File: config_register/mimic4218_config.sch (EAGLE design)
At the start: 19 parts, among them P5 44PINEDGE, U1 CD74HCT123, U2 CD74HCT123, U3 CD74HC573E, U4 CD74HC573E

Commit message: update netlist
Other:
- note added: "X_INTEN, U_INTEN, J_INTEN and ITENSIFY the cathode voltage. Low Levels bring the cathode negative. When Intensity is brought high the lectron gun will pulse"
- note added: "input"
- note added: "output"
- note added: "scale"
- note removed: "When high INTENSIFY will pulse the electron gun."
- note removed: "X_INTEN, U_INTEN, J_INTEN set the cathode voltage when the electron gun is on. Logic lows bring the cathode most negative."
- moved on the sheet: P5
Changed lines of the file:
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@@
 <text x="403.86" y="302.26" size="1.9304" layer="91" ratio="10">The J_JUMP, K_JUMP, L_JUMP bits bus to the Contra_1579 cards.
 Low levels on these lines enable current.</text>
-<text x="403.86" y="312.42" size="1.9304" layer="91" ratio="10">The DELAY_SELECT bit selects the 35 uS delay when high
+<text x="403.86" y="320.04" size="1.9304" layer="91" ratio="10">The DELAY_SELECT bit selects the 35 uS delay when high
 and the 1 uS delay when low.</text>
-<text x="403.86" y="322.58" size="1.9304" layer="91" ratio="10">When high INTENSIFY will pulse the electron gun.</text>
-<text x="403.86" y="330.2" size="1.9304" layer="91" ratio="10">X_INTEN, U_INTEN, J_INTEN set the cathode voltage
-when the electron gun is on.  Logic lows bring the
-cathode most negative.</text>
+<text x="403.86" y="330.2" size="1.9304" layer="91" ratio="10">X_INTEN, U_INTEN, J_INTEN and ITENSIFY the cathode voltage.
+Low Levels bring the cathode negative.
+When Intensity is brought high the lectron gun will pulse</text>
+<text x="134.62" y="337.82" size="1.778" layer="91">output</text>
+<text x="78.74" y="337.82" size="1.778" layer="91">input</text>
+<text x="134.62" y="337.82" size="1.778" layer="91">output</text>
+<text x="149.86" y="297.18" size="1.778" layer="91">scale</text>
+<text x="149.86" y="274.32" size="1.778" layer="91">scale</text>
 </plain>
 <instances>
@@
 <instance part="FRAME1" gate="G$1" x="0" y="0"/>
 <instance part="FRAME1" gate="G$2" x="452.12" y="0"/>
-<instance part="P5" gate="G$1" x="99.06" y="251.46"/>
+<instance part="P5" gate="G$1" x="91.44" y="251.46"/>
 <instance part="U1" gate="G$1" x="330.2" y="220.98"/>
 <instance part="U2" gate="G$1" x="330.2" y="149.86"/>
@@
 <wire x1="220.98" y1="304.8" x2="294.64" y2="304.8" width="0.1524" layer="91"/>
 <label x="220.98" y="304.8" size="1.9304" layer="95" font="vector" ratio="10" rot="MR0" xref="yes"/>
+</segment>
+<segment>
+<wire x1="81.28" y1="325.12" x2="93.98" y2="325.12" width="0.1524" layer="91"/>
+<label x="81.28" y="325.12" size="1.9304" layer="95" font="vector" ratio="10" rot="MR0" xref="yes"/>
 </segment>
 </net>
@@
 <junction x="269.24" y="340.36"/>
 </segment>
+<segment>
+<label x="88.9" y="314.96" size="1.9304" layer="95" font="vector" ratio="10" rot="MR0" xref="yes"/>
+<wire x1="88.9" y1="314.96" x2="93.98" y2="314.96" width="0.1524" layer="91"/>
+</segment>
 </net>
 <net name="D1" class="0">
@@
 <junction x="266.7" y="337.82"/>
 </segment>
+<segment>
+<label x="81.28" y="312.42" size="1.9304" layer="95" font="vector" ratio="10" rot="MR0" xref="yes"/>
+<wire x1="81.28" y1="312.42" x2="93.98" y2="312.42" width="0.1524" layer="91"/>
+</segment>
 </net>
 <net name="D2" class="0">
@@
 <junction x="264.16" y="335.28"/>
 </segment>
+<segment>
+<label x="88.9" y="309.88" size="1.9304" layer="95" font="vector" ratio="10" rot="MR0" xref="yes"/>
+<wire x1="88.9" y1="309.88" x2="93.98" y2="309.88" width="0.1524" layer="91"/>
+</segment>
 </net>
 <net name="D3" class="0">
@@
 <junction x="261.62" y="332.74"/>
 </segment>
+<segment>
+<label x="81.28" y="307.34" size="1.9304" layer="95" font="vector" ratio="10" rot="MR0" xref="yes"/>
+<wire x1="93.98" y1="307.34" x2="81.28" y2="307.34" width="0.1524" layer="91"/>
+</segment>
 </net>
 <net name="D4" class="0">
@@
 <junction x="259.08" y="330.2"/>
 </segment>
+<segment>
+<label x="88.9" y="304.8" size="1.9304" layer="95" font="vector" ratio="10" rot="MR0" xref="yes"/>
+<wire x1="93.98" y1="304.8" x2="88.9" y2="304.8" width="0.1524" layer="91"/>
+</segment>
 </net>
 <net name="D5" class="0">
@@
 <junction x="256.54" y="327.66"/>
 </segment>
+<segment>
+<label x="81.28" y="302.26" size="1.9304" layer="95" font="vector" ratio="10" rot="MR0" xref="yes"/>
+<wire x1="93.98" y1="302.26" x2="81.28" y2="302.26" width="0.1524" layer="91"/>
+</segment>
 </net>
 <net name="D6" class="0">
@@
 <junction x="254" y="325.12"/>
 </segment>
+<segment>
+<label x="88.9" y="299.72" size="1.9304" layer="95" font="vector" ratio="10" rot="MR0" xref="yes"/>
+<wire x1="88.9" y1="299.72" x2="93.98" y2="299.72" width="0.1524" layer="91"/>
+</segment>
 </net>
 <net name="D7" class="0">
@@
 <junction x="251.46" y="322.58"/>
 </segment>
+<segment>
+<label x="81.28" y="297.18" size="1.9304" layer="95" font="vector" ratio="10" rot="MR0" xref="yes"/>
+<wire x1="93.98" y1="297.18" x2="81.28" y2="297.18" width="0.1524" layer="91"/>
+</segment>
 </net>
 <net name="LE2" class="0">
@@
 <wire x1="294.64" y1="345.44" x2="220.98" y2="345.44" width="0.1524" layer="91"/>
 <label x="220.98" y="345.44" size="1.9304" layer="95" font="vector" ratio="10" rot="MR0" xref="yes"/>
+</segment>
+<segment>
+<wire x1="93.98" y1="320.04" x2="81.28" y2="320.04" width="0.1524" layer="91"/>
+<label x="81.28" y="320.04" size="1.9304" layer="95" font="vector" ratio="10" rot="MR0" xref="yes"/>
 </segment>
 </net>
@@
 </segment>
 <segment>
-<label x="144.78" y="279.4" size="1.9304" layer="95" font="vector" ratio="10" xref="yes"/>
-<wire x1="139.7" y1="279.4" x2="144.78" y2="279.4" width="0.1524" layer="91"/>
+<label x="129.54" y="327.66" size="1.9304" layer="95" font="vector" ratio="10" xref="yes"/>
+<wire x1="129.54" y1="327.66" x2="124.46" y2="327.66" width="0.1524" layer="91"/>
 </segment>
 </net>
@@
 </segment>
 <segment>
-<wire x1="139.7" y1="264.16" x2="144.78" y2="264.16" width="0.1524" layer="91"/>
-<label x="144.78" y="264.16" size="1.9304" layer="95" font="vector" ratio="10" xref="yes"/>
+<label x="129.54" y="317.5" size="1.9304" layer="95" font="vector" ratio="10" xref="yes"/>
+<wire x1="124.46" y1="317.5" x2="129.54" y2="317.5" width="0.1524" layer="91"/>
 </segment>
 </net>
@@
 </segment>
 <segment>
-<wire x1="139.7" y1="271.78" x2="144.78" y2="271.78" width="0.1524" layer="91"/>
-<label x="144.78" y="271.78" size="1.9304" layer="95" font="vector" ratio="10" xref="yes"/>
+<label x="129.54" y="322.58" size="1.9304" layer="95" font="vector" ratio="10" xref="yes"/>
+<wire x1="124.46" y1="322.58" x2="129.54" y2="322.58" width="0.1524" layer="91"/>
 </segment>
 </net>
@@
 <label x="363.22" y="332.74" size="1.9304" layer="95" font="vector" ratio="10" xref="yes"/>
 </segment>
+<segment>
+<label x="96.52" y="330.2" size="1.9304" layer="95" font="vector" ratio="10" rot="R180" xref="yes"/>
+<wire x1="96.52" y1="330.2" x2="104.14" y2="330.2" width="0.1524" layer="91"/>
+</segment>
 </net>
 <net name="J_JUMP" class="0">
@@
 </segment>
 <segment>
-<wire x1="139.7" y1="256.54" x2="144.78" y2="256.54" width="0.1524" layer="91"/>
-<label x="144.78" y="256.54" size="1.9304" layer="95" font="vector" ratio="10" xref="yes"/>
+<label x="129.54" y="302.26" size="1.9304" layer="95" font="vector" ratio="10" xref="yes"/>
+<wire x1="124.46" y1="302.26" x2="129.54" y2="302.26" width="0.1524" layer="91"/>
 </segment>
 </net>
@@
 </segment>
 <segment>
-<wire x1="139.7" y1="248.92" x2="144.78" y2="248.92" width="0.1524" layer="91"/>
-<label x="144.78" y="248.92" size="1.9304" layer="95" font="vector" ratio="10" xref="yes"/>
+<wire x1="124.46" y1="297.18" x2="129.54" y2="297.18" width="0.1524" layer="91"/>
+<label x="129.54" y="297.18" size="1.9304" layer="95" font="vector" ratio="10" xref="yes"/>
 </segment>
 </net>
@@
 </segment>
 <segment>
-<wire x1="139.7" y1="241.3" x2="144.78" y2="241.3" width="0.1524" layer="91"/>
-<label x="144.78" y="241.3" size="1.9304" layer="95" font="vector" ratio="10" xref="yes"/>
+<wire x1="124.46" y1="292.1" x2="129.54" y2="292.1" width="0.1524" layer="91"/>
+<label x="129.54" y="292.1" size="1.9304" layer="95" font="vector" ratio="10" xref="yes"/>
 </segment>
 </net>
@@
 </segment>
 <segment>
-<wire x1="139.7" y1="210.82" x2="144.78" y2="210.82" width="0.1524" layer="91"/>
-<label x="144.78" y="210.82" size="1.9304" layer="95" font="vector" ratio="10" xref="yes"/>
+<label x="129.54" y="266.7" size="1.9304" layer="95" font="vector" ratio="10" xref="yes"/>
+<wire x1="124.46" y1="266.7" x2="129.54" y2="266.7" width="0.1524" layer="91"/>
 </segment>
 </net>
@@
 </segment>
 <segment>
-<wire x1="139.7" y1="218.44" x2="144.78" y2="218.44" width="0.1524" layer="91"/>
-<label x="144.78" y="218.44" size="1.9304" layer="95" font="vector" ratio="10" xref="yes"/>
+<label x="129.54" y="271.78" size="1.9304" layer="95" font="vector" ratio="10" xref="yes"/>
+<wire x1="124.46" y1="271.78" x2="129.54" y2="271.78" width="0.1524" layer="91"/>
 </segment>
 </net>
@@
 </segment>
 <segment>
-<wire x1="139.7" y1="233.68" x2="144.78" y2="233.68" width="0.1524" layer="91"/>
-<label x="144.78" y="233.68" size="1.9304" layer="95" font="vector" ratio="10" xref="yes"/>
+<label x="129.54" y="281.94" size="1.9304" layer="95" font="vector" ratio="10" xref="yes"/>
+<wire x1="124.46" y1="281.94" x2="129.54" y2="281.94" width="0.1524" layer="91"/>
 </segment>
 </net>
@@
 </segment>
 <segment>
-<wire x1="144.78" y1="226.06" x2="139.7" y2="226.06" width="0.1524" layer="91"/>
-<label x="144.78" y="226.06" size="1.9304" layer="95" font="vector" ratio="10" xref="yes"/>
+<wire x1="129.54" y1="276.86" x2="124.46" y2="276.86" width="0.1524" layer="91"/>
+<label x="129.54" y="276.86" size="1.9304" layer="95" font="vector" ratio="10" xref="yes"/>
 </segment>
 </net>
@@
 </segment>
 <segment>
-<wire x1="144.78" y1="287.02" x2="139.7" y2="287.02" width="0.1524" layer="91"/>
-<label x="144.78" y="287.02" size="1.9304" layer="95" font="vector" xref="yes"/>
-</segment>
-</net>
+<wire x1="129.54" y1="312.42" x2="124.46" y2="312.42" width="0.1524" layer="91"/>
+<label x="129.54" y="312.42" size="1.9304" layer="95" font="vector" ratio="10" xref="yes"/>
+</segment>
+</net>

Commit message: going to lunch
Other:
- note added: "* The original DEC 4218 System Design Module was a data latch. It was used to capture some of the original DEC 340 configuration bits shown on this page."
- note added: "X_INTEN, U_INTEN, J_INTEN control cathode voltage. Low levels bring the cathode negative. INTENSITY high enables a pulse."
- note removed: "X_INTEN, U_INTEN, J_INTEN and ITENSIFY the cathode voltage. Low Levels bring the cathode negative. When Intensity is brought high the lectron gun will pulse"
- note removed: "input"
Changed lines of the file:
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@@
 <text x="373.888" y="143.764" size="1.778" layer="91">500 nS</text>
 <text x="373.888" y="159.004" size="1.778" layer="91">400 nS</text>
-<text x="226.06" y="218.44" size="1.778" layer="91">POSITIVE_EDGE</text>
+<text x="220.98" y="33.02" size="5.08" layer="91" font="vector" ratio="10">* The original DEC 4218 System Design Module
+was a data latch.  It was used to capture some
+of the original DEC 340 configuration bits shown
+on this page.</text>
 <text x="403.86" y="294.64" size="1.9304" layer="91" ratio="10">High levels to direction bits enable current drive.</text>
 <text x="403.86" y="302.26" size="1.9304" layer="91" ratio="10">The J_JUMP, K_JUMP, L_JUMP bits bus to the Contra_1579 cards.
@@
 <text x="403.86" y="320.04" size="1.9304" layer="91" ratio="10">The DELAY_SELECT bit selects the 35 uS delay when high
 and the 1 uS delay when low.</text>
-<text x="403.86" y="330.2" size="1.9304" layer="91" ratio="10">X_INTEN, U_INTEN, J_INTEN and ITENSIFY the cathode voltage.
-Low Levels bring the cathode negative.
-When Intensity is brought high the lectron gun will pulse</text>
+<text x="398.78" y="358.14" size="3.81" layer="91" font="vector" ratio="10">X_INTEN, U_INTEN, J_INTEN control cathode
+voltage.  Low levels bring the cathode
+negative.  INTENSITY high enables a pulse.</text>
 <text x="134.62" y="337.82" size="1.778" layer="91">output</text>
-<text x="78.74" y="337.82" size="1.778" layer="91">input</text>
 <text x="134.62" y="337.82" size="1.778" layer="91">output</text>
 <text x="149.86" y="297.18" size="1.778" layer="91">scale</text>
 <text x="149.86" y="274.32" size="1.778" layer="91">scale</text>
+<text x="226.06" y="220.98" size="1.778" layer="91">POSITIVE_EDGE</text>
 </plain>
 <instances>
@@
 <net name="DELAY_SELECT" class="0">
 <segment>
-<label x="236.22" y="236.22" size="1.9304" layer="95" font="vector" ratio="10" rot="R180" xref="yes"/>
-<wire x1="236.22" y1="236.22" x2="254" y2="236.22" width="0.1524" layer="91"/>
 <pinref part="U5" gate="G$1" pin="1B"/>
 <wire x1="254" y1="236.22" x2="256.54" y2="236.22" width="0.1524" layer="91"/>
@@
 <wire x1="279.4" y1="233.68" x2="274.32" y2="233.68" width="0.1524" layer="91"/>
 <pinref part="U5" gate="G$1" pin="1A"/>
-</segment>
-<segment>
 <pinref part="U4" gate="G$1" pin="Q3"/>
-<wire x1="312.42" y1="332.74" x2="363.22" y2="332.74" width="0.1524" layer="91"/>
+<wire x1="312.42" y1="332.74" x2="327.66" y2="332.74" width="0.1524" layer="91"/>
 <label x="363.22" y="332.74" size="1.9304" layer="95" font="vector" ratio="10" xref="yes"/>
 <label x="363.22" y="332.74" size="1.9304" layer="95" font="vector" ratio="10" xref="yes"/>
-</segment>
-<segment>
-<label x="96.52" y="330.2" size="1.9304" layer="95" font="vector" ratio="10" rot="R180" xref="yes"/>
-<wire x1="96.52" y1="330.2" x2="104.14" y2="330.2" width="0.1524" layer="91"/>
-</segment>
-</net>
+<wire x1="327.66" y1="332.74" x2="363.22" y2="332.74" width="0.1524" layer="91"/>
+<wire x1="279.4" y1="243.84" x2="327.66" y2="243.84" width="0.1524" layer="91"/>
+<wire x1="327.66" y1="243.84" x2="327.66" y2="332.74" width="0.1524" layer="91"/>
+<junction x="279.4" y="243.84"/>
+<junction x="327.66" y="332.74"/>
+</segment>
+</net>

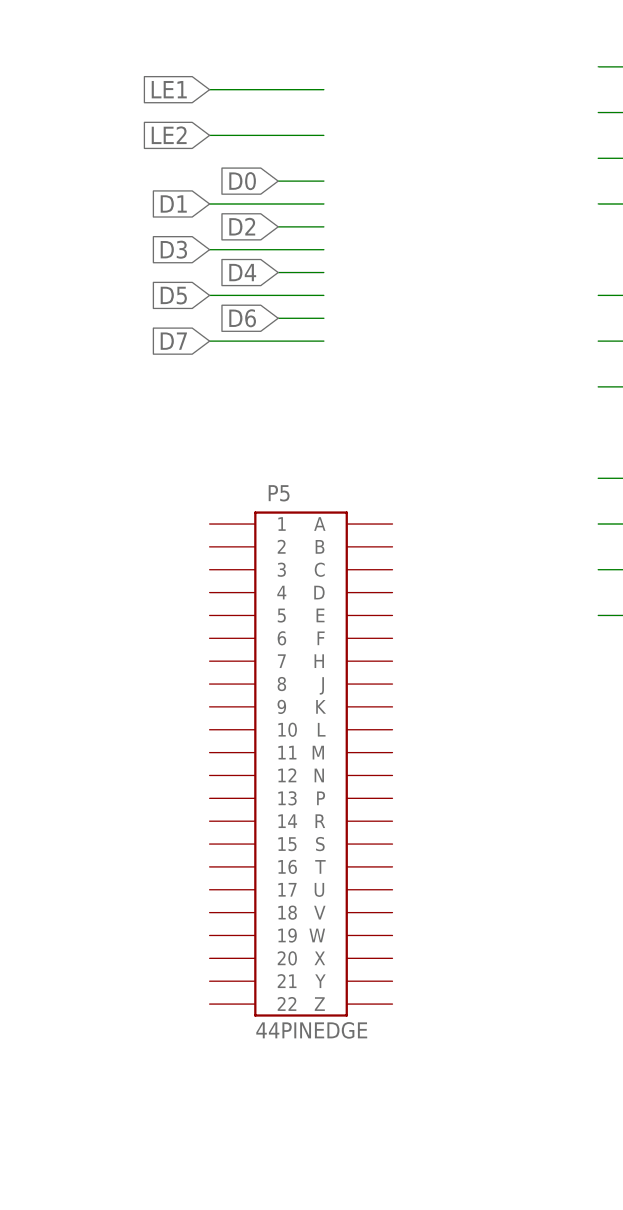
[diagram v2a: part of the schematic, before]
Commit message: D/A being routed
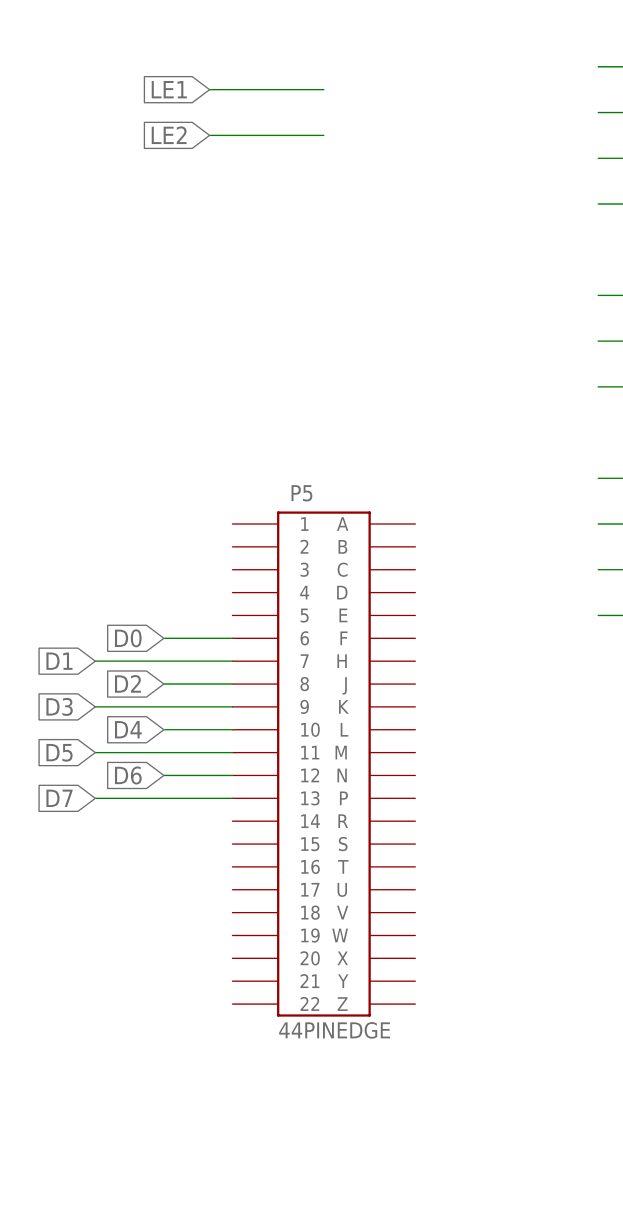
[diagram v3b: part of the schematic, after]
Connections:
- net D0: now also P5.6
- net D1: now also P5.7
- net D2: now also P5.8
- net D3: now also P5.9
- net D4: now also P5.10
- net D5: now also P5.11
- net D6: now also P5.12
- net D7: now also P5.13
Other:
- moved on the sheet: P5
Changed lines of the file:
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@@
 <instance part="FRAME1" gate="G$1" x="0" y="0"/>
 <instance part="FRAME1" gate="G$2" x="452.12" y="0"/>
-<instance part="P5" gate="G$1" x="91.44" y="251.46"/>
+<instance part="P5" gate="G$1" x="93.98" y="251.46"/>
 <instance part="U1" gate="G$1" x="330.2" y="220.98"/>
 <instance part="U2" gate="G$1" x="330.2" y="149.86"/>
@@
 </segment>
 <segment>
-<label x="88.9" y="314.96" size="1.9304" layer="95" font="vector" ratio="10" rot="MR0" xref="yes"/>
-<wire x1="88.9" y1="314.96" x2="93.98" y2="314.96" width="0.1524" layer="91"/>
+<label x="76.2" y="264.16" size="1.9304" layer="95" font="vector" ratio="10" rot="MR0" xref="yes"/>
+<wire x1="76.2" y1="264.16" x2="83.82" y2="264.16" width="0.1524" layer="91"/>
+<pinref part="P5" gate="G$1" pin="6"/>
 </segment>
 </net>
@@
 </segment>
 <segment>
-<label x="81.28" y="312.42" size="1.9304" layer="95" font="vector" ratio="10" rot="MR0" xref="yes"/>
-<wire x1="81.28" y1="312.42" x2="93.98" y2="312.42" width="0.1524" layer="91"/>
+<label x="68.58" y="261.62" size="1.9304" layer="95" font="vector" ratio="10" rot="MR0" xref="yes"/>
+<wire x1="68.58" y1="261.62" x2="83.82" y2="261.62" width="0.1524" layer="91"/>
+<pinref part="P5" gate="G$1" pin="7"/>
 </segment>
 </net>
@@
 </segment>
 <segment>
-<label x="88.9" y="309.88" size="1.9304" layer="95" font="vector" ratio="10" rot="MR0" xref="yes"/>
-<wire x1="88.9" y1="309.88" x2="93.98" y2="309.88" width="0.1524" layer="91"/>
+<label x="76.2" y="259.08" size="1.9304" layer="95" font="vector" ratio="10" rot="MR0" xref="yes"/>
+<wire x1="76.2" y1="259.08" x2="83.82" y2="259.08" width="0.1524" layer="91"/>
+<pinref part="P5" gate="G$1" pin="8"/>
 </segment>
 </net>
@@
 </segment>
 <segment>
-<label x="81.28" y="307.34" size="1.9304" layer="95" font="vector" ratio="10" rot="MR0" xref="yes"/>
-<wire x1="93.98" y1="307.34" x2="81.28" y2="307.34" width="0.1524" layer="91"/>
+<label x="68.58" y="256.54" size="1.9304" layer="95" font="vector" ratio="10" rot="MR0" xref="yes"/>
+<wire x1="83.82" y1="256.54" x2="68.58" y2="256.54" width="0.1524" layer="91"/>
+<pinref part="P5" gate="G$1" pin="9"/>
 </segment>
 </net>
@@
 </segment>
 <segment>
-<label x="88.9" y="304.8" size="1.9304" layer="95" font="vector" ratio="10" rot="MR0" xref="yes"/>
-<wire x1="93.98" y1="304.8" x2="88.9" y2="304.8" width="0.1524" layer="91"/>
+<label x="76.2" y="254" size="1.9304" layer="95" font="vector" ratio="10" rot="MR0" xref="yes"/>
+<wire x1="83.82" y1="254" x2="76.2" y2="254" width="0.1524" layer="91"/>
+<pinref part="P5" gate="G$1" pin="10"/>
 </segment>
 </net>
@@
 </segment>
 <segment>
-<label x="81.28" y="302.26" size="1.9304" layer="95" font="vector" ratio="10" rot="MR0" xref="yes"/>
-<wire x1="93.98" y1="302.26" x2="81.28" y2="302.26" width="0.1524" layer="91"/>
+<label x="68.58" y="251.46" size="1.9304" layer="95" font="vector" ratio="10" rot="MR0" xref="yes"/>
+<wire x1="83.82" y1="251.46" x2="68.58" y2="251.46" width="0.1524" layer="91"/>
+<pinref part="P5" gate="G$1" pin="11"/>
 </segment>
 </net>
@@
 </segment>
 <segment>
-<label x="88.9" y="299.72" size="1.9304" layer="95" font="vector" ratio="10" rot="MR0" xref="yes"/>
-<wire x1="88.9" y1="299.72" x2="93.98" y2="299.72" width="0.1524" layer="91"/>
+<label x="76.2" y="248.92" size="1.9304" layer="95" font="vector" ratio="10" rot="MR0" xref="yes"/>
+<wire x1="76.2" y1="248.92" x2="83.82" y2="248.92" width="0.1524" layer="91"/>
+<pinref part="P5" gate="G$1" pin="12"/>
 </segment>
 </net>
@@
 </segment>
 <segment>
-<label x="81.28" y="297.18" size="1.9304" layer="95" font="vector" ratio="10" rot="MR0" xref="yes"/>
-<wire x1="93.98" y1="297.18" x2="81.28" y2="297.18" width="0.1524" layer="91"/>
-</segment>
-</net>
+<label x="68.58" y="246.38" size="1.9304" layer="95" font="vector" ratio="10" rot="MR0" xref="yes"/>
+<wire x1="83.82" y1="246.38" x2="68.58" y2="246.38" width="0.1524" layer="91"/>
+<pinref part="P5" gate="G$1" pin="13"/>
+</segment>
+</net>
